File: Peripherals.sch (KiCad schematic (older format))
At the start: 45 parts, among them J10 Conn_01x01, J11 Conn_01x01, J12 Conn_01x01, J5 Conn_01x10, J6 Conn_01x10, J7 Conn_01x10, J8 Conn_01x08, J9 Conn_01x01, U10 74HCT32, U11 74HCT00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

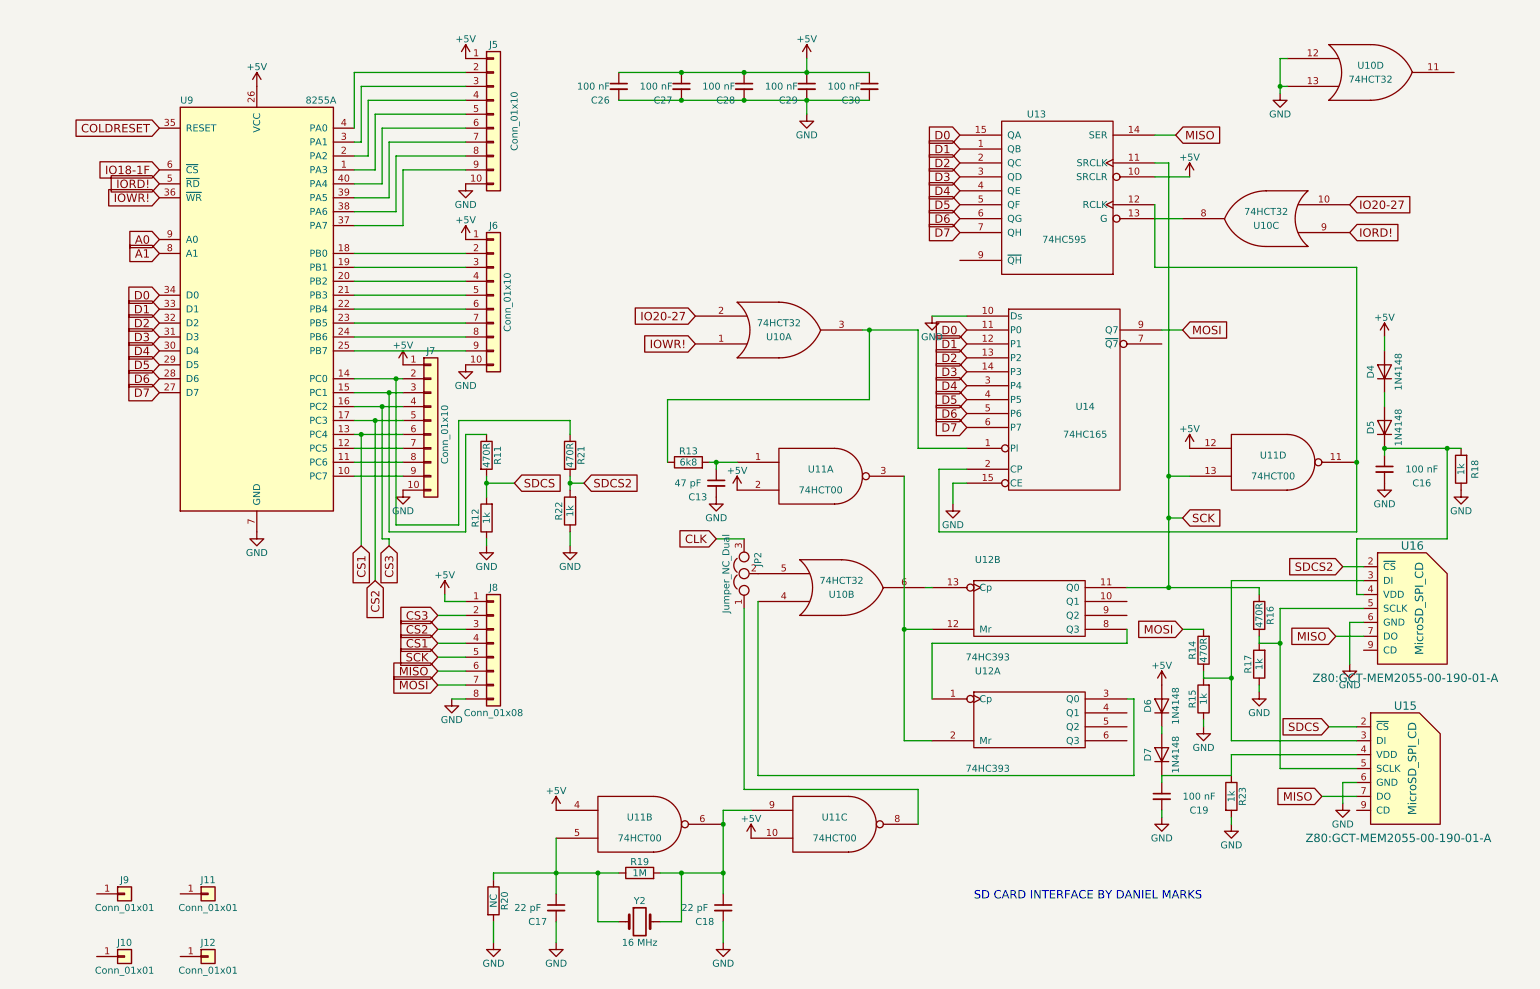
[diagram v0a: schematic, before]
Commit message: Added PS/2 keyboard input
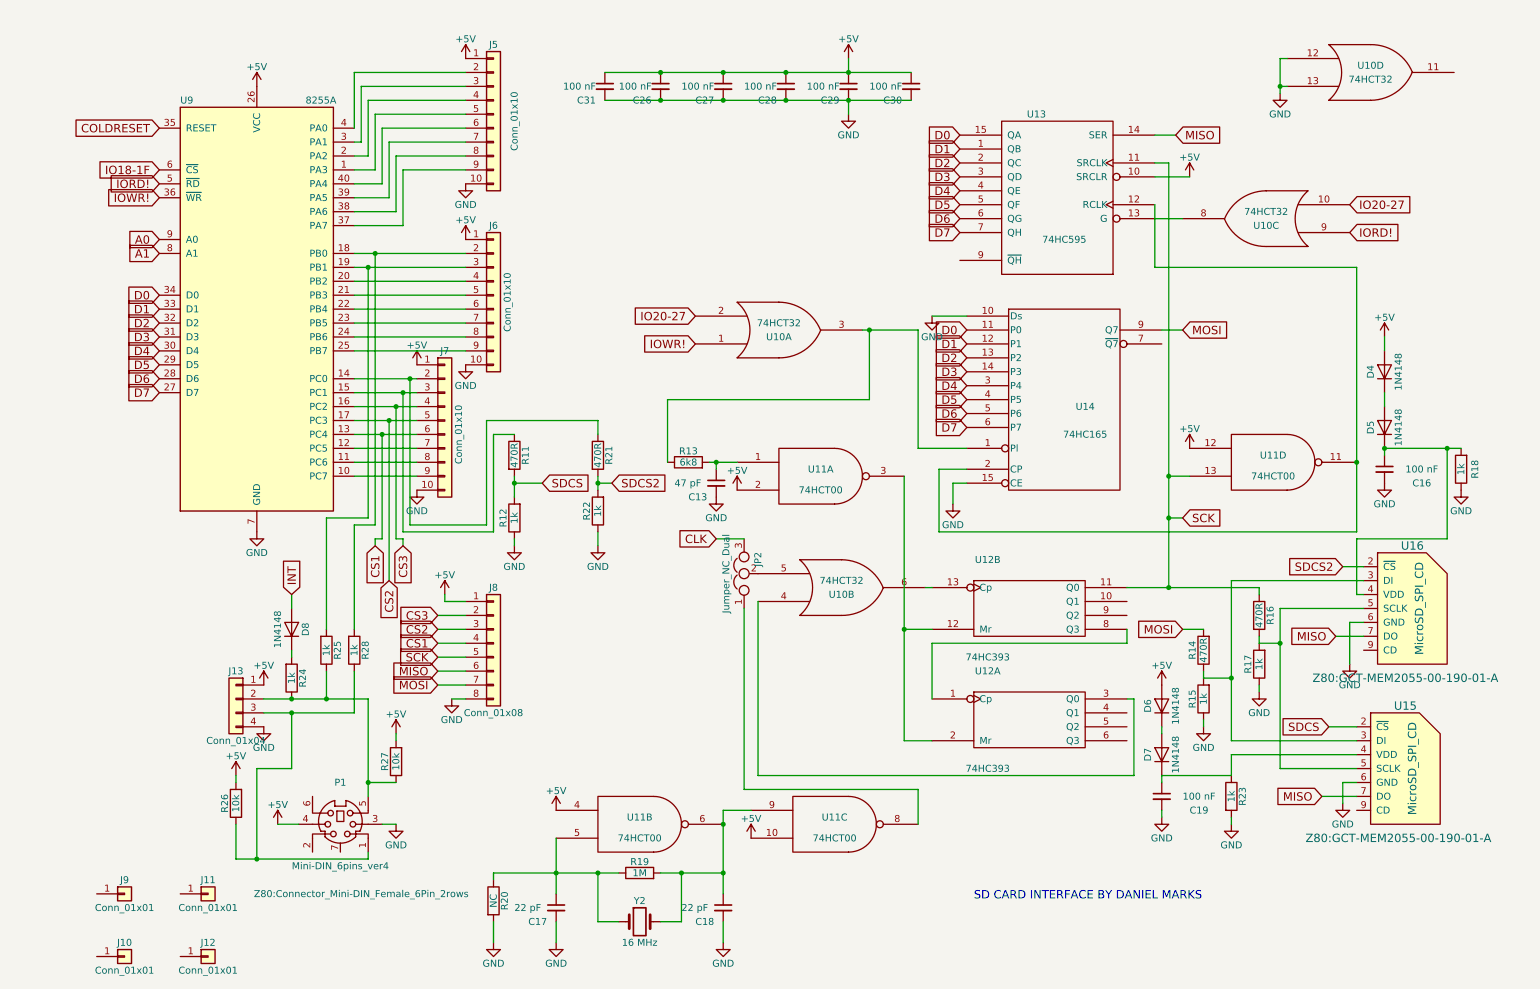
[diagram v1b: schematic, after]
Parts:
- added C31: 100 nF, Capacitors_THT:C_Disc_D5.0mm_W2.5mm_P2.50mm, symbol C_Small
- added D8: 1N4148, Diodes_THT:D_DO-35_SOD27_P7.62mm_Horizontal, symbol D
- added J13: Conn_01x04, Pin_Headers:Pin_Header_Straight_1x04_Pitch2.54mm, symbol Conn_01x04
- added P1: Mini-DIN_6pins_ver4, Z80:Connector_Mini-DIN_Female_6Pin_2rows, symbol Mini-DIN_6pins_ver4
- added R24, R25, R28: 1k, Resistors_THT:R_Axial_DIN0207_L6.3mm_D2.5mm_P7.62mm_Horizontal, symbol R
- added R26, R27: 10k, Resistors_THT:R_Axial_DIN0207_L6.3mm_D2.5mm_P7.62mm_Horizontal, symbol R
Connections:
- net +5V: now also C31.1, J13.1 (Pin_1), P1.4, R26.2, R27.2
- net GND: now also C31.2, J13.4 (Pin_4), P1.3
- net at J6.2 (Pin_2), U9.18 (PB0): now also R28.2
- net at J6.3 (Pin_3), U9.19 (PB1): now also R25.2
- new net: J13.2 (Pin_2), P1.5, R24.1, R25.1, R27.1
- new net: J13.3 (Pin_3), P1.1, R26.1, R28.1
- new net: D8.1 (K), R24.2
- new net INT: D8.2 (A)
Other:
- moved on the sheet: C26, C27, C28, C29, C30, J7, R11, R12, R21, R22

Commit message: Added ESP-01 and video output
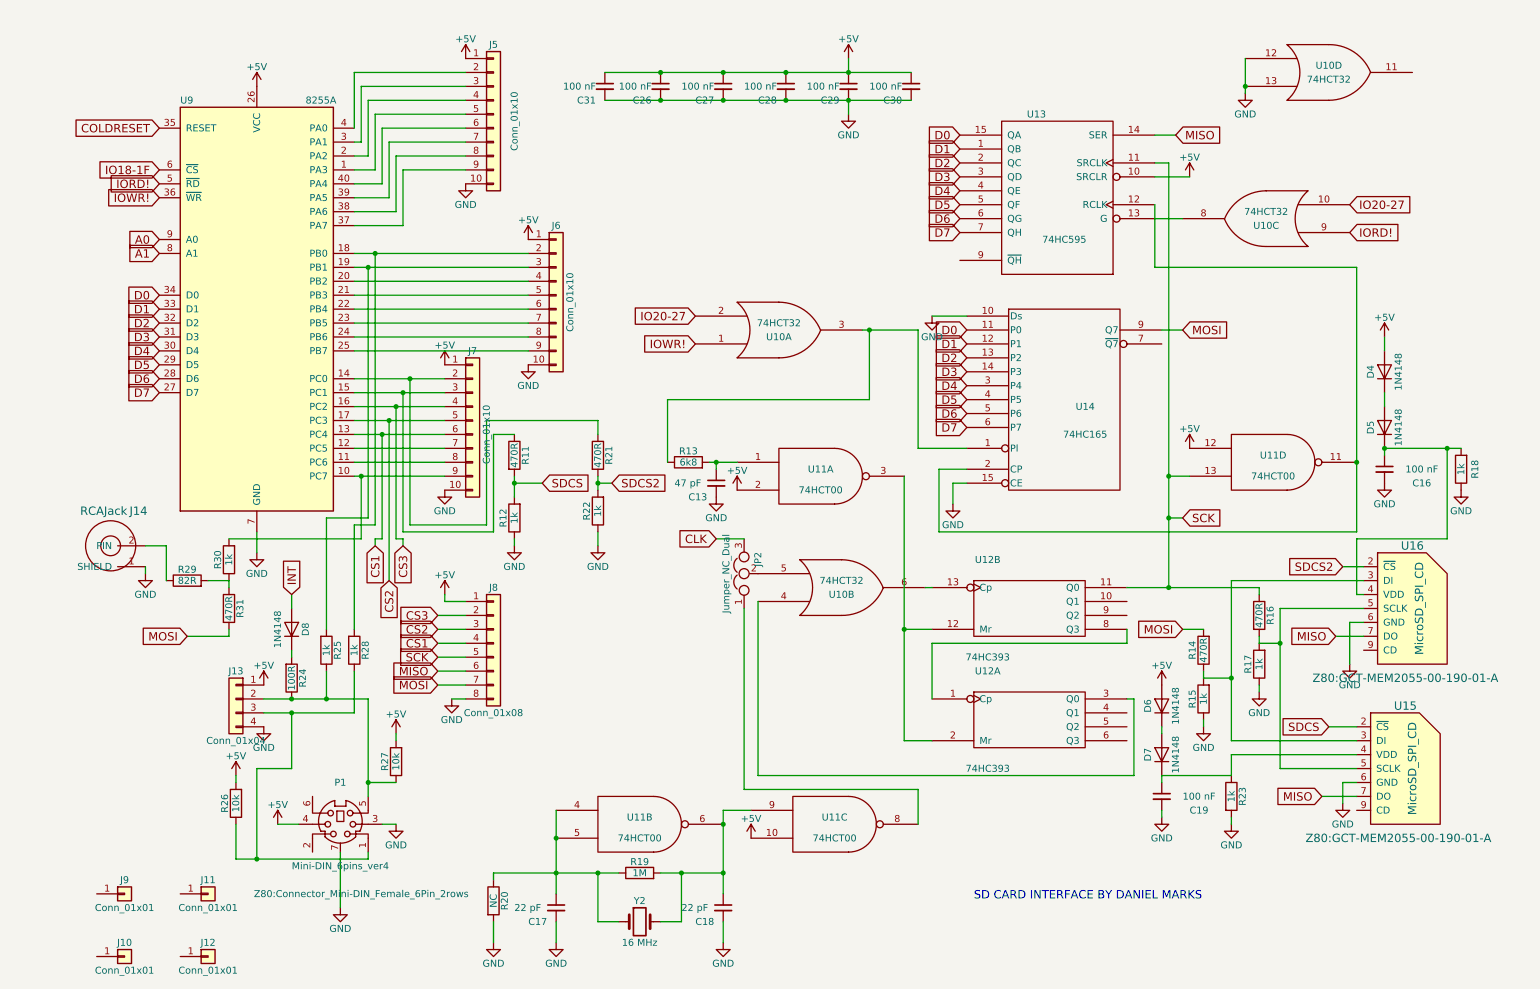
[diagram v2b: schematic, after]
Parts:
- added J14: RCAJack, Z80:RCAConnectorCommon, symbol RCAJack
- added R29: 82R, Resistors_THT:R_Axial_DIN0207_L6.3mm_D2.5mm_P7.62mm_Horizontal, symbol R
- added R30: 1k, Resistors_THT:R_Axial_DIN0207_L6.3mm_D2.5mm_P7.62mm_Horizontal, symbol R
- added R31: 470R, Resistors_THT:R_Axial_DIN0207_L6.3mm_D2.5mm_P7.62mm_Horizontal, symbol R
- R24: value 1k -> 100R
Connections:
- net +5V: no longer U11.4
- net GND: now also P1.7 (Shell), J14.1 (SHIELD)
- net MOSI: now also R31.2
- net at C17.1, R19.1, R20.1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: now also U11.4
- net at J7.9 (Pin_9), U9.10 (PC7): now also R30.2
- new net: R29.2, R30.1, R31.1
- new net: J14.2 (PIN), R29.1
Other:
- moved on the sheet: J6, J7, U10D

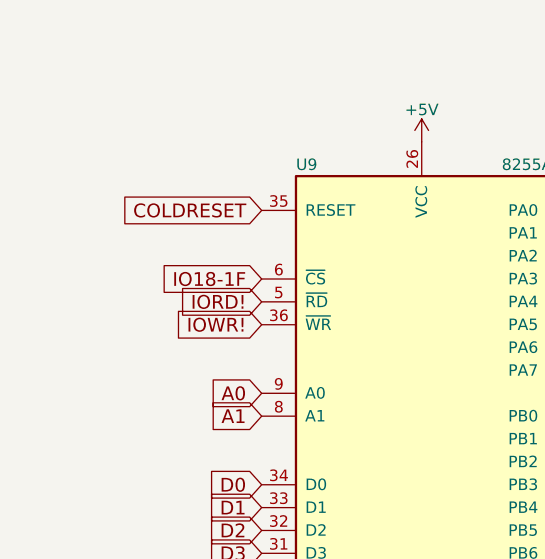
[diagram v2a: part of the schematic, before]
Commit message: Fixed jumpers, CF card position, ESP-01 enable
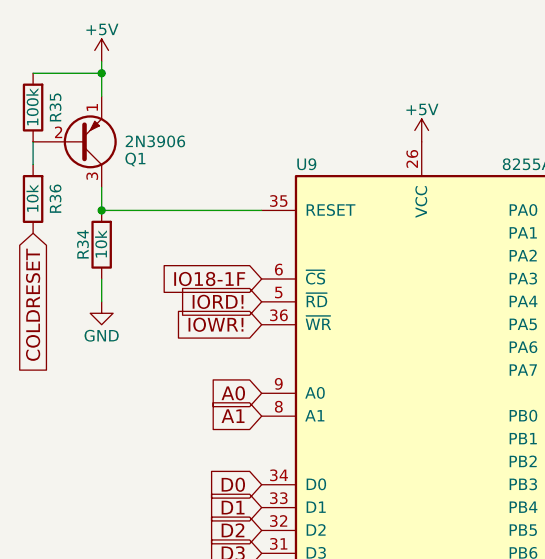
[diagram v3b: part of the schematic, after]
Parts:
- added Q1: 2N3906, TO_SOT_Packages_THT:TO-92_Inline_Wide, symbol 2N3906
- added R34, R36: 10k, Resistors_THT:R_Axial_DIN0207_L6.3mm_D2.5mm_P7.62mm_Horizontal, symbol R
- added R35: 100k, Resistors_THT:R_Axial_DIN0207_L6.3mm_D2.5mm_P7.62mm_Horizontal, symbol R
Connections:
- net +5V: now also Q1.1 (E), R35.2
- net COLDRESET: now also R36.1; no longer U9.35 (RESET)
- net GND: now also R34.1
- new net: Q1.3 (C), R34.2, U9.35 (RESET)
- new net: Q1.2 (B), R35.1, R36.2
